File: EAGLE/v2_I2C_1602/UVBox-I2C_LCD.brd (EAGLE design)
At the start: 100 x 52.6 mm, 58 parts, among them IC1 ULN2003AD, Q1 16M, Q2 BC817, SW1 Start, SW2 Mode, SW3 Add, SW4 Sub, U1 7812DT, U2 7805DT

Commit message: 細微修改
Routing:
- net GND: track 388.1 -> 389.0 mm
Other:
- outline, holes or cut-outs redrawn
- board text added: "+5V"
- board text added: "D/P"
- board text added: "JP1 : 1&2=12v 2&3=19v"
- board text added: "U/P"
- board text added: "UV Box v2 Rev:C 2016/07/21"
- board text removed: "+5V out"
- board text removed: "Dn Panel"
- board text removed: "JP1 : Output Voltage 1 + 2 = 12 2 + 3 = 19"
- board text removed: "UV Box v2 Rev:C 21 Jul, 2016"
- board text removed: "Up Panel"

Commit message: 細微修改
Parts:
- added C12: 104, rcl:C0603
- moved Q2 33.2 mm to (74.7, 46.7), flipped to the top
- moved RN1 21.5 mm to (41.7, 19.1), turned to 180 degrees
- moved C9 15.0 mm to (33.8, 30.2), flipped to the bottom, turned to 0 degrees
- moved R9 11.0 mm to (96.5, 16.8), turned to 90 degrees
- moved R8 10.6 mm to (35.6, 9.40), turned to 90 degrees
- moved U$1 9.14 mm to (68.6, 11.2)
- moved U$3 9.14 mm to (81.3, 11.2)
- moved R5 4.26 mm to (47.2, 27.9), turned to 180 degrees
- moved R6 2.59 mm to (47.2, 26.4), turned to 180 degrees
- moved C8 2.17 mm to (36.6, 20.6), turned to 90 degrees
- moved U$2 1.02 mm to (78.0, 20.3)
- moved VR1 0.76 mm to (63.0, 48.0)
- moved VR2 0.76 mm to (69.8, 48.0)
- turned D2 to 90 degrees
- turned SG1 to 270 degrees
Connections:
- net N$29 renamed IC2P3
- removed net N$14: LCD.A, Q2.C
- new net LCD_A: LCD.A, Q2.E
- net +5V: now also C12.2
- net GND: now also C12.1, LCD.K; no longer Q2.E, VR1.1, VR2.1
- net KEY1: now also RN1.4; no longer RN1.1
- net KEY2: now also RN1.3; no longer RN1.2
- net KEY3: now also RN1.2; no longer RN1.3
- net KEY4: now also RN1.1; no longer RN1.4
- net N$12: now also Q2.C; no longer LCD.K
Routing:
- net GND: track 389.0 -> 1.01 mm, vias 25 -> 29
- net LCD_A: track 0.00 -> 29.2 mm
- net N$14: track 19.2 -> 0.00 mm
- net !DTR: track 22.2 -> 6.12 mm, vias 1 -> 0
- net RESET: track 77.0 -> 61.2 mm
- net +5V: track 395.4 -> 410.1 mm, vias 6 -> 3
- net KEY1: track 30.8 -> 16.5 mm, vias 0 -> 2
- net PANEL_VCC: track 97.9 -> 110.9 mm
- net IC2P3: track 29.0 -> 40.6 mm, vias 2 -> 1
- net TO_BUZZER: track 47.7 -> 36.9 mm
- net KEY3: track 33.9 -> 44.6 mm, vias 0 -> 2
- net N$12: track 15.1 -> 4.90 mm
- net N$18: track 8.35 -> 16.8 mm
- net 12V: track 43.7 -> 35.6 mm
- net KEY4: track 47.1 -> 54.5 mm
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
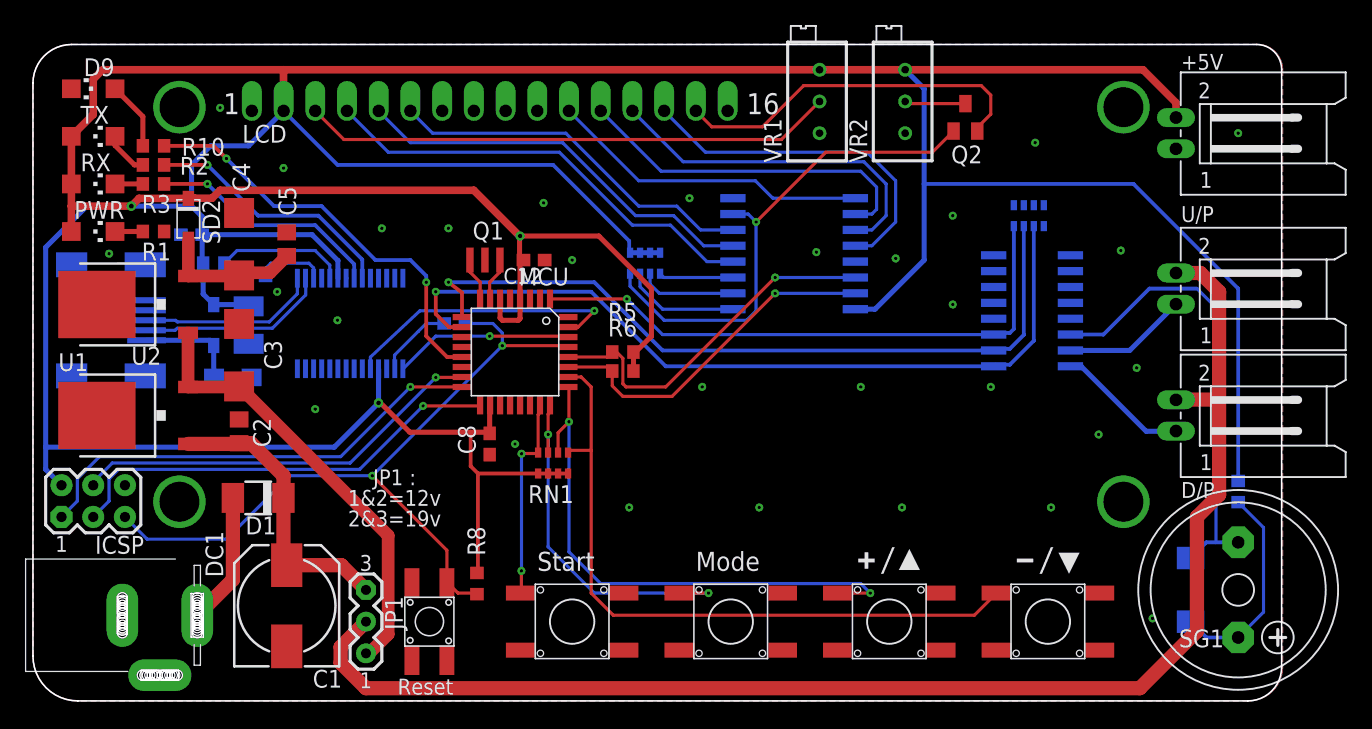
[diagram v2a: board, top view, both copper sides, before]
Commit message: 調整線路配置
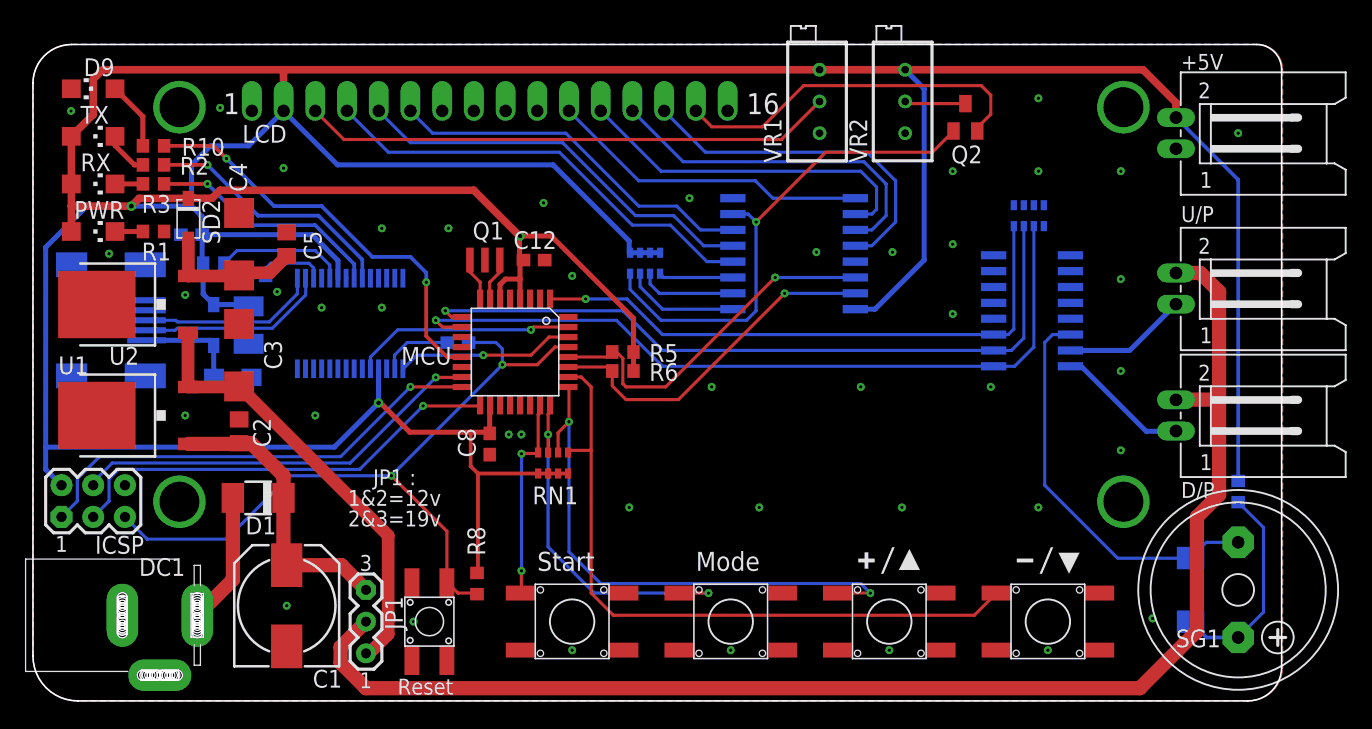
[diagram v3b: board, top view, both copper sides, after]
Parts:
- IC2: value (none) -> PCF8574
- LCD: value (none) -> HD44780
- moved C9 1.55 mm to (34.0, 28.7)
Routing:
- net +5V: track 410.1 -> 392.0 mm
- net TX: track 23.0 -> 17.8 mm
- net TO_BUZZER: track 36.9 -> 32.2 mm
- net DOWN_PANEL: track 64.7 -> 62.1 mm
- net UP_PANEL: track 60.9 -> 58.6 mm
- net RESET: track 61.2 -> 60.2 mm
- net GND: vias 29 -> 43
